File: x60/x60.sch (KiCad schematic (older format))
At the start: 141 parts, among them SW1 SW_Push, U1 ATmega32U4-AU, Y1 16mhz

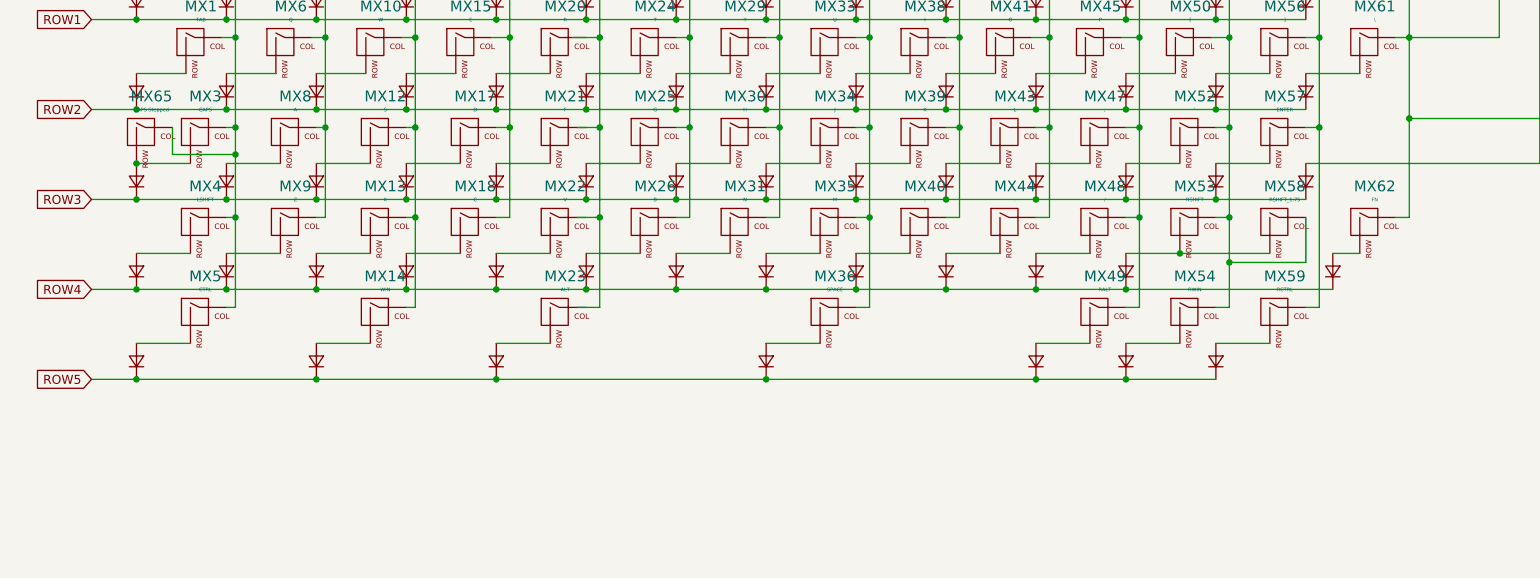
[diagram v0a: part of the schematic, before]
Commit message: added 1.25u bottom row support
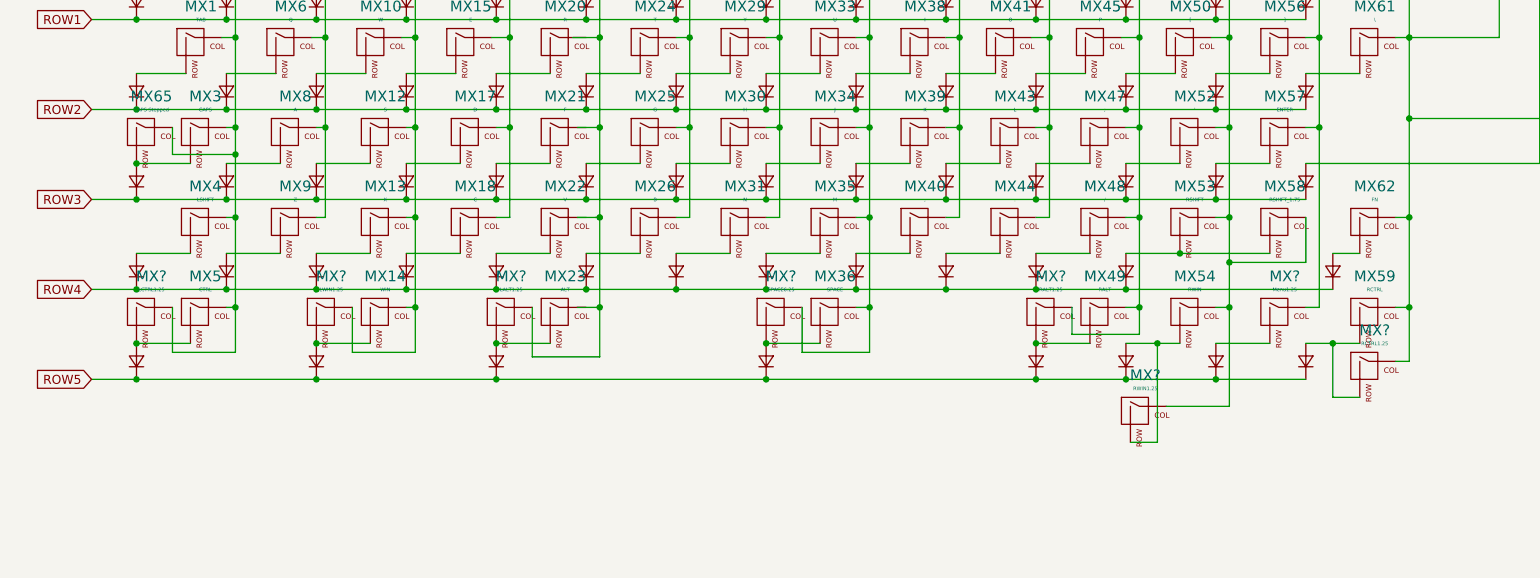
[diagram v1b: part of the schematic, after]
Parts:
- added D?: D_Small, Diode_SMD:D_SOD-123, symbol Device:D_Small
- added MX?: LCTRL1.25, MX_Only:MXOnly-1.5U-NoLED, symbol MX_Alps_Hybrid:MX-NoLED
- added MX?: LWIN1.25, MX_Only:MXOnly-1U-NoLED, symbol MX_Alps_Hybrid:MX-NoLED
- added MX?: LALT1.25, MX_Only:MXOnly-1.5U-NoLED, symbol MX_Alps_Hybrid:MX-NoLED
- added MX?: SPACE6.25, MX_Only:MXOnly-7U-NoLED, symbol MX_Alps_Hybrid:MX-NoLED
- added MX?: RALT1.25, MX_Only:MXOnly-1.5U-NoLED, symbol MX_Alps_Hybrid:MX-NoLED
- added MX?: RWIN1.25, MX_Only:MXOnly-1U-NoLED, symbol MX_Alps_Hybrid:MX-NoLED
- added MX?: RCTRL1.25, MX_Only:MXOnly-1.5U-NoLED, symbol MX_Alps_Hybrid:MX-NoLED
- added MX?: Menu1.25, MX_Only:MXOnly-1.5U-NoLED, symbol MX_Alps_Hybrid:MX-NoLED
- MX61: footprint MX_Only:MXOnly-1U-NoLED -> MX_Only:MXOnly-1.5U-NoLED
- MX65: footprint MX_Only:MXOnly-1.5U-NoLED -> MX_Only:MXOnly-1.25U-NoLED
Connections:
- net COL1: now also MX?.1 (COL)
- net COL11: now also MX?.1 (COL)
- net COL12: now also MX?.1 (COL)
- net COL13: now also MX?.1 (COL); no longer MX59.1 (COL)
- net COL14: now also MX59.1 (COL), MX?.1 (COL)
- net COL3: now also MX?.1 (COL)
- net COL5: now also MX?.1 (COL)
- net COL8: now also MX?.1 (COL)
- net ROW5: now also D?.1 (K)
- net at D5.2 (A), MX5.2 (ROW): now also MX?.2 (ROW)
- net at D14.2 (A), MX14.2 (ROW): now also MX?.2 (ROW)
- net at D23.2 (A), MX23.2 (ROW): now also MX?.2 (ROW)
- net at D36.2 (A), MX36.2 (ROW): now also MX?.2 (ROW)
- net at D49.2 (A), MX49.2 (ROW): now also MX?.2 (ROW)
- net at D54.2 (A), MX54.2 (ROW): now also MX?.2 (ROW)
- net at MX59.2 (ROW): now also D?.2 (A), MX?.2 (ROW); no longer D58.2 (A)
- new net: D58.2 (A), MX?.2 (ROW)
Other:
- moved on the sheet: MX59
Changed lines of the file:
@@
 	10050 3000 9750 3000
 Wire Wire Line
-	10550 3000 10250 3000
-Wire Wire Line
-	11050 3000 10750 3000
+	10550 3000 10425 3000
 $Comp
 L Device:D_Small D58
@@
 Wire Wire Line
 	11250 1000 11550 1000
-Connection ~ 11325 1800
-Wire Wire Line
-	11325 2800 11325 1800
-Wire Wire Line
-	11250 2800 11325 2800
 Wire Wire Line
 	11325 1300 11325 800
@@
 L MX_Alps_Hybrid:MX-NoLED MX59
 U 1 1 6188008D
-P 11100 2850
-F 0 "MX59" H 11133 3073 60  0000 C CNN
-F 1 "RCTRL" H 11133 2999 20  0000 C CNN
-F 2 "MX_Only:MXOnly-1.5U-NoLED" H 10475 2825 60  0001 C CNN
-F 3 "" H 10475 2825 60  0001 C CNN
-	1    11100 2850
+P 11600 2850
+F 0 "MX59" H 11633 3073 60  0000 C CNN
+F 1 "RCTRL" H 11633 2999 20  0000 C CNN
+F 2 "MX_Only:MXOnly-1.5U-NoLED" H 10975 2825 60  0001 C CNN
+F 3 "" H 10975 2825 60  0001 C CNN
+	1    11600 2850
 	1    0    0    -1
 $EndComp
@@
 F 0 "MX61" H 11633 1573 60  0000 C CNN
 F 1 "\\" H 11633 1499 20  0000 C CNN
-F 2 "MX_Only:MXOnly-1U-NoLED" H 10975 1325 60  0001 C CNN
+F 2 "MX_Only:MXOnly-1.5U-NoLED" H 10975 1325 60  0001 C CNN
 F 3 "" H 10975 1325 60  0001 C CNN
 	1    11600 1350
@@
 F 0 "MX65" H 4833 2073 60  0000 C CNN
 F 1 "CAPS Stepped" H 4833 1999 20  0000 C CNN
-F 2 "MX_Only:MXOnly-1.5U-NoLED" H 4175 1825 60  0001 C CNN
+F 2 "MX_Only:MXOnly-1.25U-NoLED" H 4175 1825 60  0001 C CNN
 F 3 "" H 4175 1825 60  0001 C CNN
 	1    4800 1850
@@
 	1    0    0    -1
 $EndComp
+$Comp
+L MX_Alps_Hybrid:MX-NoLED MX?
+U 1 1 619A1AC8
+P 4800 2850
+F 0 "MX?" H 4833 3073 60  0000 C CNN
+F 1 "LCTRL1.25" H 4833 2999 20  0000 C CNN
+F 2 "MX_Only:MXOnly-1.5U-NoLED" H 4175 2825 60  0001 C CNN
+F 3 "" H 4175 2825 60  0001 C CNN
+	1    4800 2850
+	1    0    0    -1
+$EndComp
+Connection ~ 4750 3000
+Wire Wire Line
+	4950 2800 4950 3050
+Wire Wire Line
+	4950 3050 5300 3050
+Wire Wire Line
+	5300 3050 5300 2800
+Connection ~ 5300 2800
+$Comp
+L MX_Alps_Hybrid:MX-NoLED MX?
+U 1 1 619C1D52
+P 5800 2850
+F 0 "MX?" H 5833 3073 60  0000 C CNN
+F 1 "LWIN1.25" H 5833 2999 20  0000 C CNN
+F 2 "MX_Only:MXOnly-1U-NoLED" H 5175 2825 60  0001 C CNN
+F 3 "" H 5175 2825 60  0001 C CNN
+	1    5800 2850
+	1    0    0    -1
+$EndComp
+Connection ~ 5750 3000
+Wire Wire Line
+	5950 2800 5950 3050
+Wire Wire Line
+	5950 3050 6300 3050
+Wire Wire Line
+	6300 3050 6300 2800
+Connection ~ 6300 2800
+$Comp
+L MX_Alps_Hybrid:MX-NoLED MX?
+U 1 1 619E258F
+P 6800 2850
+F 0 "MX?" H 6833 3073 60  0000 C CNN
+F 1 "LALT1.25" H 6833 2999 20  0000 C CNN
+F 2 "MX_Only:MXOnly-1.5U-NoLED" H 6175 2825 60  0001 C CNN
+F 3 "" H 6175 2825 60  0001 C CNN
+	1    6800 2850
+	1    0    0    -1
+$EndComp
+Connection ~ 6750 3000
+Wire Wire Line
+	6950 2800 6950 3075
+Wire Wire Line
+	6950 3075 7325 3075
+Wire Wire Line
+	7325 3075 7325 2800
+Connection ~ 7325 2800
+$Comp
+L MX_Alps_Hybrid:MX-NoLED MX?
+U 1 1 61A0358B
+P 8300 2850
+F 0 "MX?" H 8333 3073 60  0000 C CNN
+F 1 "SPACE6.25" H 8333 2999 20  0000 C CNN
+F 2 "MX_Only:MXOnly-7U-NoLED" H 7675 2825 60  0001 C CNN
+F 3 "" H 7675 2825 60  0001 C CNN
+	1    8300 2850
+	1    0    0    -1
+$EndComp
+Connection ~ 8250 3000
+Wire Wire Line
+	8450 2800 8450 3050
+Wire Wire Line
+	8450 3050 8825 3050
+Wire Wire Line
+	8825 3050 8825 2800
+Connection ~ 8825 2800
+$Comp
+L MX_Alps_Hybrid:MX-NoLED MX?
+U 1 1 61A24F68
+P 9800 2850
+F 0 "MX?" H 9833 3073 60  0000 C CNN
+F 1 "RALT1.25" H 9833 2999 20  0000 C CNN
+F 2 "MX_Only:MXOnly-1.5U-NoLED" H 9175 2825 60  0001 C CNN
+F 3 "" H 9175 2825 60  0001 C CNN
+	1    9800 2850
+	1    0    0    -1
+$EndComp
+Connection ~ 9750 3000
+Wire Wire Line
+	9950 2800 9950 2950
+Wire Wire Line
+	9950 2950 10325 2950
+Wire Wire Line
+	10325 2950 10325 2800
+Connection ~ 10325 2800
+$Comp
+L MX_Alps_Hybrid:MX-NoLED MX?
+U 1 1 61A46A5C
+P 10325 3400
+F 0 "MX?" H 10358 3623 60  0000 C CNN
+F 1 "RWIN1.25" H 10358 3549 20  0000 C CNN
+F 2 "MX_Only:MXOnly-1U-NoLED" H 9700 3375 60  0001 C CNN
+F 3 "" H 9700 3375 60  0001 C CNN
+	1    10325 3400
+	1    0    0    -1
+$EndComp
+Wire Wire Line
+	10275 3550 10425 3550
+Wire Wire Line
+	10425 3550 10425 3000
+Connection ~ 10425 3000
+Wire Wire Line
+	10425 3000 10250 3000
+Wire Wire Line
+	10475 3350 10825 3350
+Wire Wire Line
+	10825 3350 10825 2800
+Connection ~ 10825 2800
+$Comp
+L MX_Alps_Hybrid:MX-NoLED MX?
+U 1 1 61A8C732
+P 11600 3150
+F 0 "MX?" H 11633 3373 60  0000 C CNN
+F 1 "RCTRL1.25" H 11633 3299 20  0000 C CNN
+F 2 "MX_Only:MXOnly-1.5U-NoLED" H 10975 3125 60  0001 C CNN
+F 3 "" H 10975 3125 60  0001 C CNN
+	1    11600 3150
+	1    0    0    -1
+$EndComp
+Wire Wire Line
+	11825 2300 11825 2800
+Wire Wire Line
+	11825 2800 11750 2800
+Connection ~ 11825 2300
+Wire Wire Line
+	11550 3000 11400 3000
+$Comp
+L Device:D_Small D?
+U 1 1 61AF5B94
+P 11250 3100
+F 0 "D?" H 11350 3250 50  0001 R CNN
+F 1 "D_Small" H 11550 3175 50  0001 R CNN
+F 2 "Diode_SMD:D_SOD-123" V 11250 3100 50  0001 C CNN
+F 3 "~" V 11250 3100 50  0001 C CNN
+	1    11250 3100
+	0    -1   -1   0
+$EndComp
+Wire Wire Line
+	11250 3200 10750 3200
+Connection ~ 10750 3200
+Wire Wire Line
+	11550 3300 11400 3300
+Wire Wire Line
+	11400 3300 11400 3000
+Connection ~ 11400 3000
+Wire Wire Line
+	11400 3000 11250 3000
+Wire Wire Line
+	11750 3100 11825 3100
+Wire Wire Line
+	11825 3100 11825 2800
+Connection ~ 11825 2800
+$Comp
+L MX_Alps_Hybrid:MX-NoLED MX?
+U 1 1 61B5EE3E
+P 11100 2850
+F 0 "MX?" H 11133 3073 60  0000 C CNN
+F 1 "Menu1.25" H 11133 2999 20  0000 C CNN
+F 2 "MX_Only:MXOnly-1.5U-NoLED" H 10475 2825 60  0001 C CNN
+F 3 "" H 10475 2825 60  0001 C CNN
+	1    11100 2850
+	1    0    0    -1
+$EndComp
+Wire Wire Line
+	11050 3000 10750 3000
+Wire Wire Line
+	11325 1800 11325 2800
+Wire Wire Line
+	11325 2800 11250 2800
+Connection ~ 11325 1800
 $EndSCHEMATC

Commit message: wired and arranged 1.25u bottom row
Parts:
- MX66, MX68, MX70, MX72, MX73: renamed from MX?; footprint MX_Only:MXOnly-1.5U-NoLED -> MX_Only:MXOnly-1.25U-NoLED
- MX67, MX71: renamed from MX?; footprint MX_Only:MXOnly-1U-NoLED -> MX_Only:MXOnly-1.25U-NoLED
- MX69: renamed from MX?; footprint MX_Only:MXOnly-7U-NoLED -> MX_Only:MXOnly-6.25U-NoLED
- gave numbers to parts that had none: 1
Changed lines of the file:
@@
 $EndComp
 $Comp
-L MX_Alps_Hybrid:MX-NoLED MX?
+L MX_Alps_Hybrid:MX-NoLED MX66
 U 1 1 619A1AC8
 P 4800 2850
-F 0 "MX?" H 4833 3073 60  0000 C CNN
+F 0 "MX66" H 4833 3073 60  0000 C CNN
 F 1 "LCTRL1.25" H 4833 2999 20  0000 C CNN
-F 2 "MX_Only:MXOnly-1.5U-NoLED" H 4175 2825 60  0001 C CNN
+F 2 "MX_Only:MXOnly-1.25U-NoLED" H 4175 2825 60  0001 C CNN
 F 3 "" H 4175 2825 60  0001 C CNN
 	1    4800 2850
@@
 Connection ~ 5300 2800
 $Comp
-L MX_Alps_Hybrid:MX-NoLED MX?
+L MX_Alps_Hybrid:MX-NoLED MX67
 U 1 1 619C1D52
 P 5800 2850
-F 0 "MX?" H 5833 3073 60  0000 C CNN
+F 0 "MX67" H 5833 3073 60  0000 C CNN
 F 1 "LWIN1.25" H 5833 2999 20  0000 C CNN
-F 2 "MX_Only:MXOnly-1U-NoLED" H 5175 2825 60  0001 C CNN
+F 2 "MX_Only:MXOnly-1.25U-NoLED" H 5175 2825 60  0001 C CNN
 F 3 "" H 5175 2825 60  0001 C CNN
 	1    5800 2850
@@
 Connection ~ 6300 2800
 $Comp
-L MX_Alps_Hybrid:MX-NoLED MX?
+L MX_Alps_Hybrid:MX-NoLED MX68
 U 1 1 619E258F
 P 6800 2850
-F 0 "MX?" H 6833 3073 60  0000 C CNN
+F 0 "MX68" H 6833 3073 60  0000 C CNN
 F 1 "LALT1.25" H 6833 2999 20  0000 C CNN
-F 2 "MX_Only:MXOnly-1.5U-NoLED" H 6175 2825 60  0001 C CNN
+F 2 "MX_Only:MXOnly-1.25U-NoLED" H 6175 2825 60  0001 C CNN
 F 3 "" H 6175 2825 60  0001 C CNN
 	1    6800 2850
@@
 Connection ~ 7325 2800
 $Comp
-L MX_Alps_Hybrid:MX-NoLED MX?
+L MX_Alps_Hybrid:MX-NoLED MX69
 U 1 1 61A0358B
 P 8300 2850
-F 0 "MX?" H 8333 3073 60  0000 C CNN
+F 0 "MX69" H 8333 3073 60  0000 C CNN
 F 1 "SPACE6.25" H 8333 2999 20  0000 C CNN
-F 2 "MX_Only:MXOnly-7U-NoLED" H 7675 2825 60  0001 C CNN
+F 2 "MX_Only:MXOnly-6.25U-NoLED" H 7675 2825 60  0001 C CNN
 F 3 "" H 7675 2825 60  0001 C CNN
 	1    8300 2850
@@
 Connection ~ 8825 2800
 $Comp
-L MX_Alps_Hybrid:MX-NoLED MX?
+L MX_Alps_Hybrid:MX-NoLED MX70
 U 1 1 61A24F68
 P 9800 2850
-F 0 "MX?" H 9833 3073 60  0000 C CNN
+F 0 "MX70" H 9833 3073 60  0000 C CNN
 F 1 "RALT1.25" H 9833 2999 20  0000 C CNN
-F 2 "MX_Only:MXOnly-1.5U-NoLED" H 9175 2825 60  0001 C CNN
+F 2 "MX_Only:MXOnly-1.25U-NoLED" H 9175 2825 60  0001 C CNN
 F 3 "" H 9175 2825 60  0001 C CNN
 	1    9800 2850
@@
 Connection ~ 10325 2800
 $Comp
-L MX_Alps_Hybrid:MX-NoLED MX?
+L MX_Alps_Hybrid:MX-NoLED MX71
 U 1 1 61A46A5C
 P 10325 3400
-F 0 "MX?" H 10358 3623 60  0000 C CNN
+F 0 "MX71" H 10358 3623 60  0000 C CNN
 F 1 "RWIN1.25" H 10358 3549 20  0000 C CNN
-F 2 "MX_Only:MXOnly-1U-NoLED" H 9700 3375 60  0001 C CNN
+F 2 "MX_Only:MXOnly-1.25U-NoLED" H 9700 3375 60  0001 C CNN
 F 3 "" H 9700 3375 60  0001 C CNN
 	1    10325 3400
@@
 Connection ~ 10825 2800
 $Comp
-L MX_Alps_Hybrid:MX-NoLED MX?
+L MX_Alps_Hybrid:MX-NoLED MX73
 U 1 1 61A8C732
 P 11600 3150
-F 0 "MX?" H 11633 3373 60  0000 C CNN
+F 0 "MX73" H 11633 3373 60  0000 C CNN
 F 1 "RCTRL1.25" H 11633 3299 20  0000 C CNN
-F 2 "MX_Only:MXOnly-1.5U-NoLED" H 10975 3125 60  0001 C CNN
+F 2 "MX_Only:MXOnly-1.25U-NoLED" H 10975 3125 60  0001 C CNN
 F 3 "" H 10975 3125 60  0001 C CNN
 	1    11600 3150
@@
 	11550 3000 11400 3000
 $Comp
-L Device:D_Small D?
+L Device:D_Small D63
 U 1 1 61AF5B94
 P 11250 3100
-F 0 "D?" H 11350 3250 50  0001 R CNN
+F 0 "D63" H 11350 3250 50  0001 R CNN
 F 1 "D_Small" H 11550 3175 50  0001 R CNN
 F 2 "Diode_SMD:D_SOD-123" V 11250 3100 50  0001 C CNN
@@
 Connection ~ 11825 2800
 $Comp
-L MX_Alps_Hybrid:MX-NoLED MX?
+L MX_Alps_Hybrid:MX-NoLED MX72
 U 1 1 61B5EE3E
 P 11100 2850
-F 0 "MX?" H 11133 3073 60  0000 C CNN
+F 0 "MX72" H 11133 3073 60  0000 C CNN
 F 1 "Menu1.25" H 11133 2999 20  0000 C CNN
-F 2 "MX_Only:MXOnly-1.5U-NoLED" H 10475 2825 60  0001 C CNN
+F 2 "MX_Only:MXOnly-1.25U-NoLED" H 10475 2825 60  0001 C CNN
 F 3 "" H 10475 2825 60  0001 C CNN
 	1    11100 2850

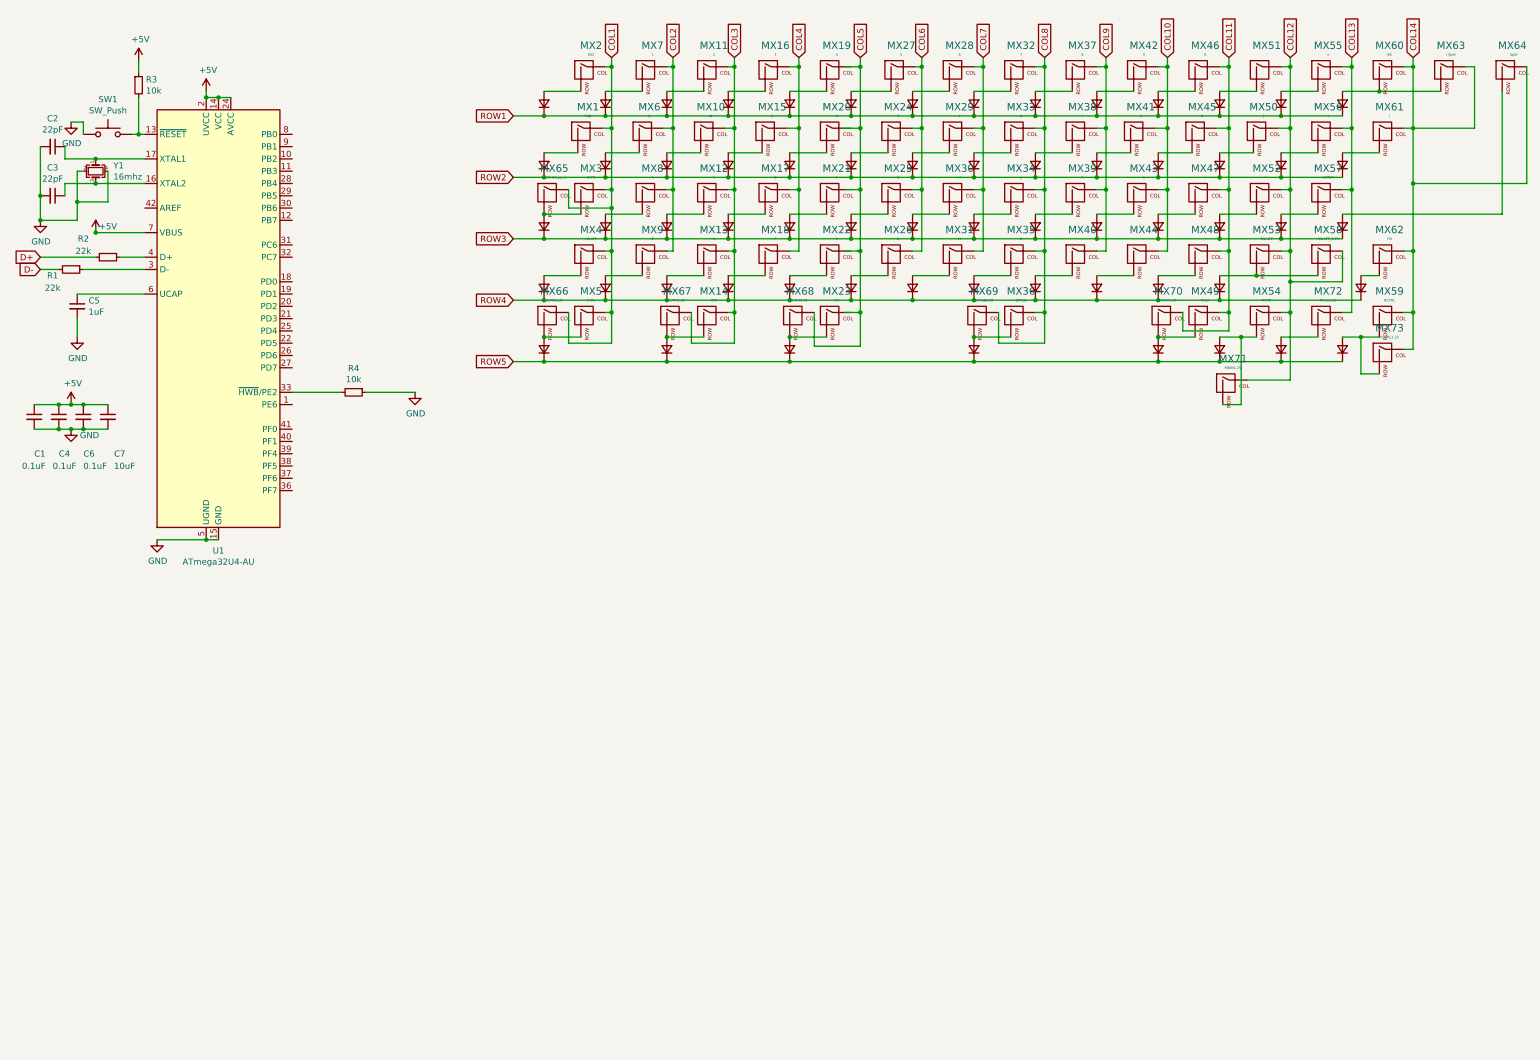
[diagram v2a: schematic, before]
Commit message: adjusted diodes top row
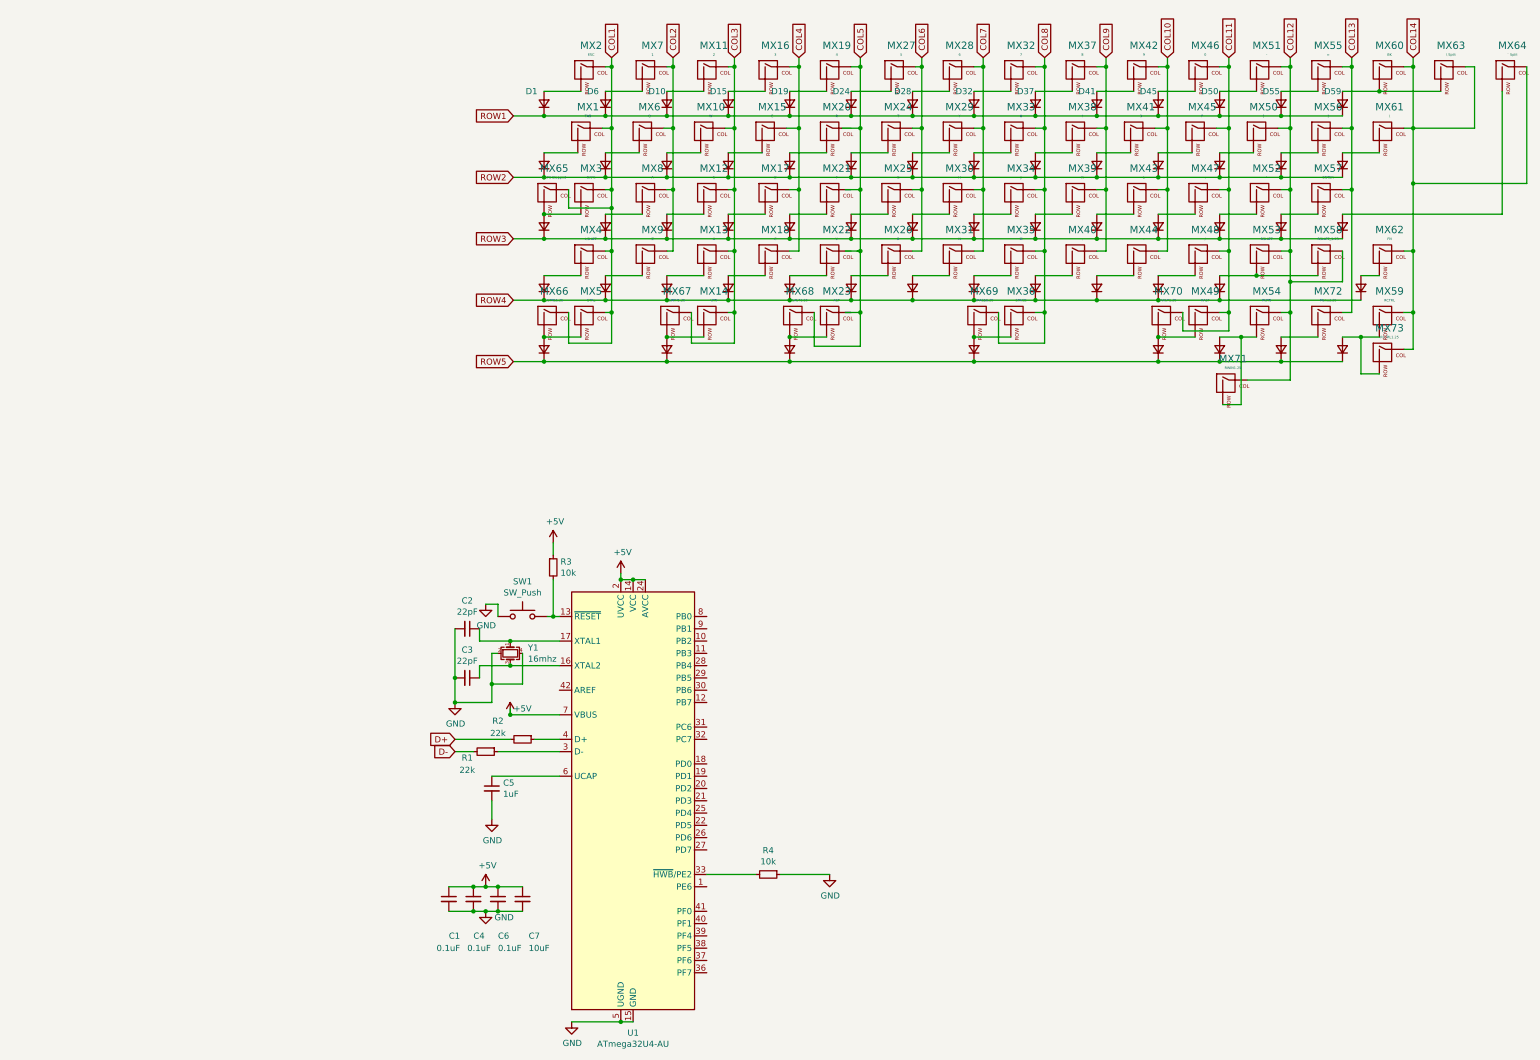
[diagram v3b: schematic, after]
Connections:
- net COL5: now also MX19.1 (COL)
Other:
- moved on the sheet: C1, C2, C3, C4, C5, C6, C7, R1, R2, R3, R4, SW1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
